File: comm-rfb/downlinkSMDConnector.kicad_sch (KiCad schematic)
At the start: 2 parts

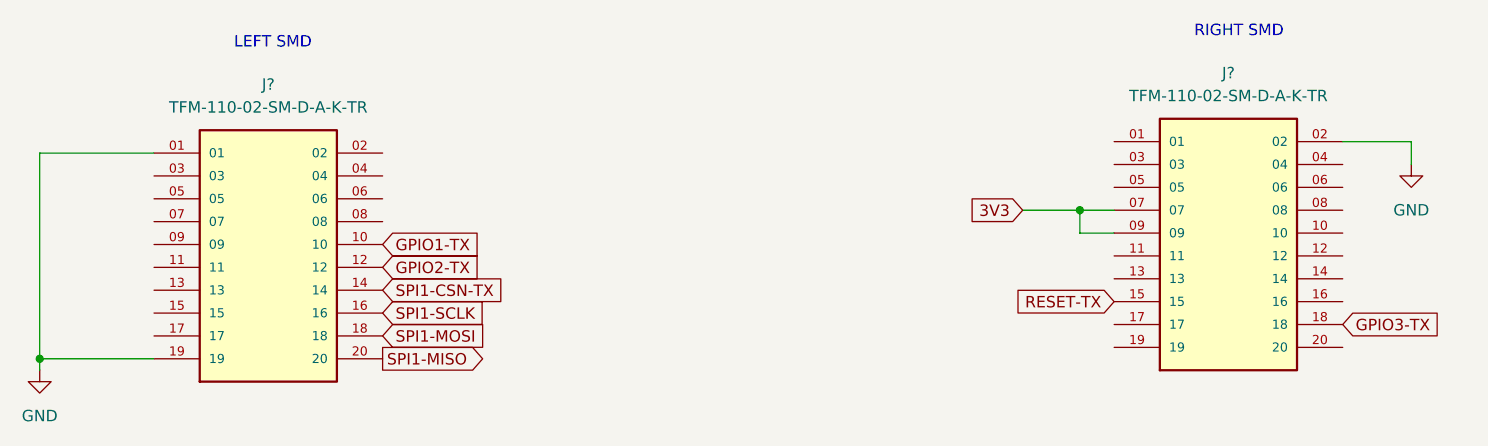
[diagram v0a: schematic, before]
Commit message: added mcu connections
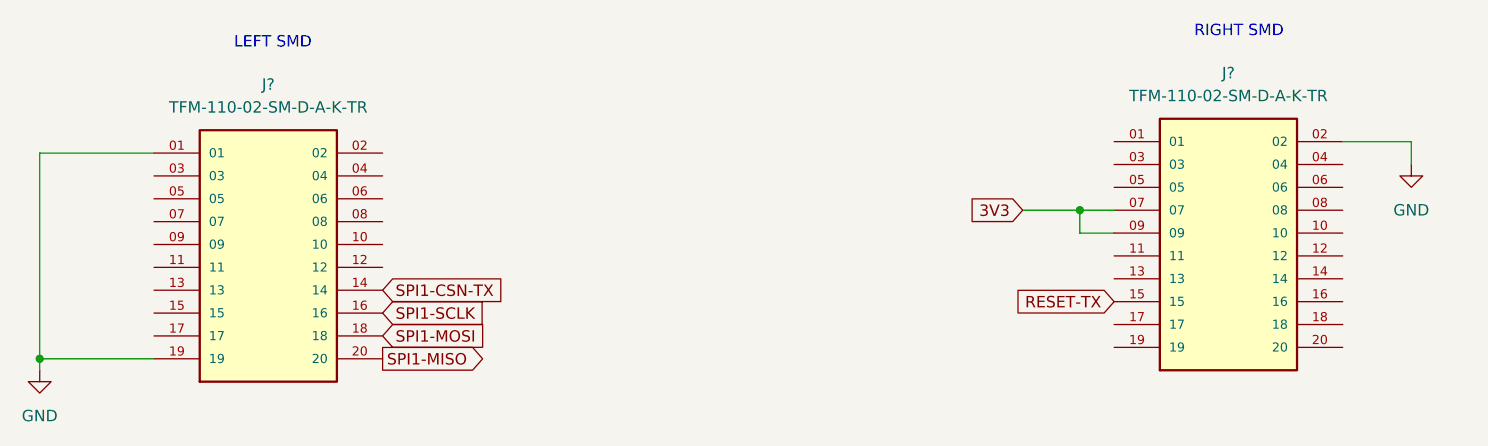
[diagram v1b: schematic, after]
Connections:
- net GPIO1-TX: no longer names the net of J?.10
- net GPIO2-TX: no longer names the net of J?.12
- net GPIO3-TX: no longer names the net of J?.18
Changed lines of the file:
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@@
     (effects (font (size 1.27 1.27)) (justify left bottom))
-  )
-  (global_label "GPIO1-TX" (shape input) (at 97.79 80.01 0) (fields_autoplaced)
-    (effects (font (size 1.27 1.27)) (justify left))
-    (property "Intersheet References" "${INTERSHEET_REFS}" (id 0) (at 109.6374 79.9306 0)
-      (effects (font (size 1.27 1.27)) (justify left) hide)
-    )
-  )
-  (global_label "GPIO3-TX" (shape input) (at 204.47 88.9 0) (fields_autoplaced)
-    (effects (font (size 1.27 1.27)) (justify left))
-    (property "Intersheet References" "${INTERSHEET_REFS}" (id 0) (at 216.3174 88.8206 0)
-      (effects (font (size 1.27 1.27)) (justify left) hide)
-    )
   )
   (global_label "3V3" (shape input) (at 168.91 76.2 180) (fields_autoplaced)
@@
       (effects (font (size 1.27 1.27)) (justify left) hide)
     )
-  )
-  (global_label "GPIO2-TX" (shape input) (at 97.79 82.55 0) (fields_autoplaced)
-    (effects (font (size 1.27 1.27)) (justify left))
-    (property "Intersheet References" "${INTERSHEET_REFS}" (id 0) (at 109.6374 82.4706 0)
-      (effects (font (size 1.27 1.27)) (justify left) hide)
-    )

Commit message: comm-rfb: reformat main schematic page
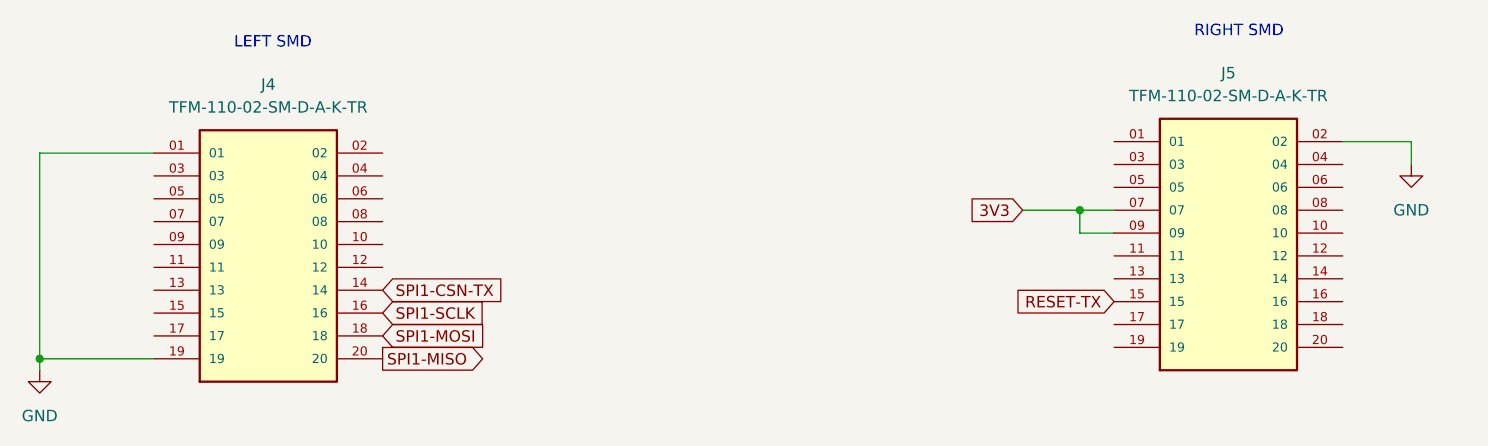
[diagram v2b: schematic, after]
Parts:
- gave numbers to parts that had none: 2
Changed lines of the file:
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@@
   (symbol (lib_id "TFM-110-02-SM-D-A-K-TR:TFM-110-02-SM-D-A-K-TR") (at 85.09 82.55 0) (unit 1)
     (in_bom yes) (on_board yes) (fields_autoplaced)
-    (property "Reference" "J?" (id 0) (at 85.09 62.23 0))
+    (property "Reference" "J4" (id 0) (at 85.09 62.23 0))
     (property "Value" "TFM-110-02-SM-D-A-K-TR" (id 1) (at 85.09 64.77 0))
     (property "Footprint" "SAMTEC_TFM-110-02-SM-D-A-K-TR" (id 2) (at 85.09 82.55 0)
@@
   (symbol (lib_id "power:GND") (at 59.69 93.98 0) (unit 1)
     (in_bom yes) (on_board yes) (fields_autoplaced)
-    (property "Reference" "#PWR?" (id 0) (at 59.69 100.33 0)
+    (property "Reference" "#PWR03" (id 0) (at 59.69 100.33 0)
       (effects (font (size 1.27 1.27)) hide)
     )
@@
   (symbol (lib_id "power:GND") (at 212.09 71.12 0) (unit 1)
     (in_bom yes) (on_board yes) (fields_autoplaced)
-    (property "Reference" "#PWR?" (id 0) (at 212.09 77.47 0)
+    (property "Reference" "#PWR04" (id 0) (at 212.09 77.47 0)
       (effects (font (size 1.27 1.27)) hide)
     )
@@
   (symbol (lib_id "TFM-110-02-SM-D-A-K-TR:TFM-110-02-SM-D-A-K-TR") (at 191.77 81.28 0) (unit 1)
     (in_bom yes) (on_board yes) (fields_autoplaced)
-    (property "Reference" "J?" (id 0) (at 191.77 60.96 0))
+    (property "Reference" "J5" (id 0) (at 191.77 60.96 0))
     (property "Value" "TFM-110-02-SM-D-A-K-TR" (id 1) (at 191.77 63.5 0))
     (property "Footprint" "SAMTEC_TFM-110-02-SM-D-A-K-TR" (id 2) (at 191.77 81.28 0)
